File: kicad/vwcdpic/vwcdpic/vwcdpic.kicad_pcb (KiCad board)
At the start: 2 copper layers, 14.6 x 13.1 mm, 11 parts, among them U1 PIC12F629, U2 LM78L05ACZ

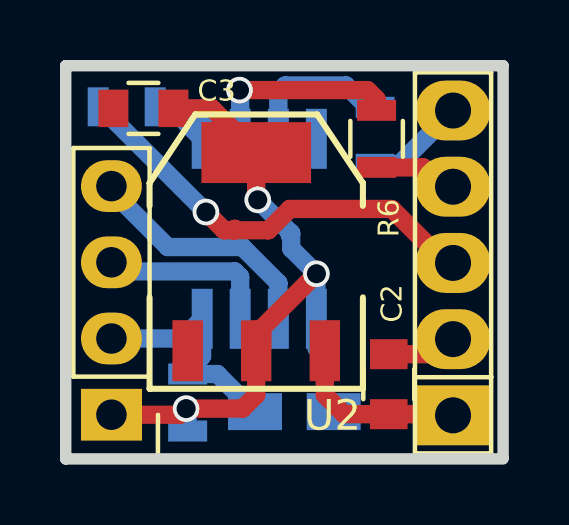
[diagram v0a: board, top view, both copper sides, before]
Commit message: 78L05 int SOT23 package as alternative to AM1117
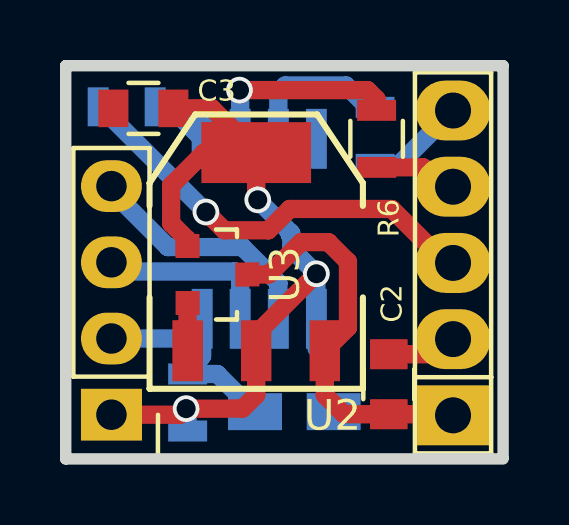
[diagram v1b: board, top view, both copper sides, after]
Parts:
- added U3: MC78L05ACH, Housings_SOT-23_SOT-143_TSOT-6:SOT-23, F.Cu at (142.8, 121.3)
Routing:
- net POWER_CTL: track 6.18 -> 13.5 mm
- net +5V: track 21.9 -> 27.5 mm
- net GND: track 2.40 -> 3.99 mm
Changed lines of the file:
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@@
-(kicad_pcb (version 4) (host pcbnew 0.201508250901+6122~28~ubuntu14.04.1-product)
+(kicad_pcb (version 4) (host pcbnew 0.201510080346+6253~30~ubuntu14.04.1-product)
   (general
-    (links 23)
+    (links 26)
     (no_connects 0)
     (area 137.579099 114.160299 152.539701 127.647701)
     (thickness 1.6002)
     (drawings 6)
-    (tracks 85)
+    (tracks 96)
     (zones 0)
-    (modules 11)
+    (modules 12)
     (nets 13)
   )
@@
     (34 B.Paste user hide)
     (35 F.Paste user hide)
-    (36 B.SilkS user hide)
+    (36 B.SilkS user)
     (37 F.SilkS user)
-    (38 B.Mask user hide)
-    (39 F.Mask user hide)
+    (38 B.Mask user)
+    (39 F.Mask user)
     (40 Dwgs.User user)
     (44 Edge.Cuts user)
@@
     (pad 5 thru_hole oval (at 5.08 0 90) (size 2 2.5) (drill 1.2) (layers *.Cu *.Mask F.SilkS)
       (net 11 CLK-PRG_DATA))
-    (model Pin_Headers/Pin_Header_Straight_1x05.wrl
+    (model Pin_Headers.3dshapes/Pin_Header_Straight_1x05.wrl
       (at (xyz 0 0 0))
       (scale (xyz 1 1 1))
@@
     (pad 4 smd rect (at 1.905 -3 180) (size 0.7 2) (layers Back B.Paste B.Mask)
       (net 8 RESET))
-    (model smd/cms_so8.wrl
-      (at (xyz 0 0 0))
-      (scale (xyz 0.5 0.32 0.5))
+    (model Housings_SOIC.3dshapes/SOIJ-8_5.3x5.3mm_Pitch1.27mm.wrl
+      (at (xyz 0 0 0))
+      (scale (xyz 1 1 1))
       (rotate (xyz 0 0 0))
     )
@@
     (pad GND smd rect (at -2.286 3.302) (size 1.016 2.032) (layers Front F.Paste F.Mask)
       (net 2 GND))
-    (model smd/SOT223.wrl
-      (at (xyz 0 0 0))
-      (scale (xyz 0.4 0.4 0.4))
+    (model /home/nail/src/kicad/KiCad/3d_models/ab2_sot/AB2_SOT223.wrl
+      (at (xyz 0 0 0))
+      (scale (xyz 1 1 1))
+      (rotate (xyz 0 0 0))
+    )
+  )
+  (module Housings_SOT-23_SOT-143_TSOT-6:SOT-23 (layer Front)
+    (at 142.82928 121.3104 270)
+    (descr "SOT-23, Standard")
+    (tags SOT-23)
+    (attr smd)
+    (fp_text reference U3 (at 0 -2.25 270) (layer F.SilkS)
+      (effects (font (size 1 1) (thickness 0.15)))
+    )
+    (fp_text value MC78L05ACH (at 0 2.3 270) (layer F.Fab)
+      (effects (font (size 1 1) (thickness 0.15)))
+    )
+    (fp_line (start -1.65 -1.6) (end 1.65 -1.6) (layer F.CrtYd) (width 0.05))
+    (fp_line (start 1.65 -1.6) (end 1.65 1.6) (layer F.CrtYd) (width 0.05))
+    (fp_line (start 1.65 1.6) (end -1.65 1.6) (layer F.CrtYd) (width 0.05))
+    (fp_line (start -1.65 1.6) (end -1.65 -1.6) (layer F.CrtYd) (width 0.05))
+    (fp_line (start 1.29916 -0.65024) (end 1.2509 -0.65024) (layer F.SilkS) (width 0.15))
+    (fp_line (start -1.49982 0.0508) (end -1.49982 -0.65024) (layer F.SilkS) (width 0.15))
+    (fp_line (start -1.49982 -0.65024) (end -1.2509 -0.65024) (layer F.SilkS) (width 0.15))
+    (fp_line (start 1.29916 -0.65024) (end 1.49982 -0.65024) (layer F.SilkS) (width 0.15))
+    (fp_line (start 1.49982 -0.65024) (end 1.49982 0.0508) (layer F.SilkS) (width 0.15))
+    (pad 1 smd rect (at -0.95 1.00076 270) (size 0.8001 0.8001) (layers Front F.Paste F.Mask)
+      (net 1 +5V))
+    (pad 2 smd rect (at 0.95 1.00076 270) (size 0.8001 0.8001) (layers Front F.Paste F.Mask)
+      (net 2 GND))
+    (pad 3 smd rect (at 0 -0.99822 270) (size 0.8001 0.8001) (layers Front F.Paste F.Mask)
+      (net 3 POWER_CTL))
+    (model Housings_SOT-23_SOT-143_TSOT-6.3dshapes/SOT-23.wrl
+      (at (xyz 0 0 0))
+      (scale (xyz 1 1 1))
       (rotate (xyz 0 0 0))
     )
@@
   (gr_line (start 137.7696 114.3508) (end 152.3492 114.3508) (angle 90) (layer Edge.Cuts) (width 0.381))
   (gr_line (start 152.3492 114.3508) (end 152.3492 127.4064) (angle 90) (layer Edge.Cuts) (width 0.381))
+  (segment (start 141.82852 120.3604) (end 141.82852 120.14708) (width 0.6096) (layer Front) (net 1) (status C00000))
+  (segment (start 141.82852 120.14708) (end 141.28496 119.60352) (width 0.6096) (layer Front) (net 1) (status 400000))
+  (segment (start 141.28496 119.60352) (end 141.28496 118.34368) (width 0.6096) (layer Front) (net 1))
+  (segment (start 141.28496 118.34368) (end 142.38224 117.2464) (width 0.6096) (layer Front) (net 1) (status 800000))
+  (segment (start 142.38224 117.2464) (end 144.1196 117.2464) (width 0.6096) (layer Front) (net 1) (status C00000))
   (segment (start 141.3604 115.7732) (end 142.6464 115.7732) (width 0.6096) (layer Front) (net 1))
   (segment (start 142.6464 115.7732) (end 144.1196 117.2464) (width 0.6096) (layer Front) (net 1))
@@
   (via (at 141.7828 125.7808) (size 0.889) (drill 0.635) (layers Front Back) (net 1))
   (segment (start 141.5796 125.984) (end 141.7828 125.7808) (width 0.6096) (layer Front) (net 1))
+  (segment (start 141.82852 122.2604) (end 141.82852 123.84532) (width 0.6096) (layer Front) (net 2) (status C00000))
+  (segment (start 141.82852 123.84532) (end 141.8336 123.8504) (width 0.6096) (layer Front) (net 2) (status C00000))
   (segment (start 148.5392 123.968) (end 150.17674 123.968) (width 0.6096) (layer Front) (net 2))
   (segment (start 150.17674 123.968) (end 150.68042 123.46432) (width 0.6096) (layer Front) (net 2))
   (segment (start 141.8336 123.7996) (end 141.8336 123.8504) (width 0.6096) (layer Front) (net 2))
+  (segment (start 143.8275 121.3104) (end 144.53616 121.3104) (width 0.6096) (layer Front) (net 3) (status 400000))
+  (segment (start 147.17776 123.07824) (end 146.4056 123.8504) (width 0.6096) (layer Front) (net 3) (status 800000))
+  (segment (start 147.17776 120.88368) (end 147.17776 123.07824) (width 0.6096) (layer Front) (net 3))
+  (segment (start 146.52752 120.23344) (end 147.17776 120.88368) (width 0.6096) (layer Front) (net 3))
+  (segment (start 145.61312 120.23344) (end 146.52752 120.23344) (width 0.6096) (layer Front) (net 3))
+  (segment (start 144.53616 121.3104) (end 145.61312 120.23344) (width 0.6096) (layer Front) (net 3))
   (segment (start 148.5392 125.968) (end 150.6441 125.968) (width 0.6096) (layer Front) (net 3))
   (segment (start 150.6441 125.968) (end 150.68042 126.00432) (width 0.6096) (layer Front) (net 3))
@@
   (segment (start 141.2522 115.7224) (end 142.3162 116.7864) (width 0.6096) (layer Back) (net 4))
   (segment (start 140.7516 115.7224) (end 141.2522 115.7224) (width 0.6096) (layer Back) (net 4))
-  (segment (start 138.8516 115.7224) (end 138.938 115.7224) (width 0.6096) (layer Back) (net 5))
+  (segment (start 142.4432 119.2276) (end 142.44828 119.2276) (width 0.6096) (layer Front) (net 5))
+  (segment (start 143.05788 119.8372) (end 144.526 119.8372) (width 0.6096) (layer Front) (net 5))
+  (segment (start 142.44828 119.2276) (end 143.05788 119.8372) (width 0.6096) (layer Front) (net 5))
   (segment (start 138.938 115.7224) (end 142.4432 119.2276) (width 0.6096) (layer Back) (net 5))
-  (segment (start 143.4084 119.7864) (end 143.4084 119.8372) (width 0.6096) (layer Front) (net 5))
-  (segment (start 143.3576 119.8372) (end 143.4084 119.7864) (width 0.6096) (layer Front) (net 5))
-  (segment (start 143.0528 119.8372) (end 143.3576 119.8372) (width 0.6096) (layer Front) (net 5))
-  (segment (start 142.4432 119.2276) (end 143.0528 119.8372) (width 0.6096) (layer Front) (net 5))
   (via (at 142.4432 119.2276) (size 0.889) (drill 0.635) (layers Front Back) (net 5))
-  (segment (start 150.68042 120.92432) (end 150.43912 120.92432) (width 0.6096) (layer Front) (net 5))
   (segment (start 150.43912 120.92432) (end 148.6408 119.126) (width 0.6096) (layer Front) (net 5))
-  (segment (start 144.526 119.8372) (end 143.4084 119.8372) (width 0.6096) (layer Front) (net 5))
   (segment (start 145.2372 119.126) (end 144.526 119.8372) (width 0.6096) (layer Front) (net 5))
   (segment (start 148.6408 119.126) (end 145.2372 119.126) (width 0.6096) (layer Front) (net 5))
+  (segment (start 138.8516 115.7224) (end 138.938 115.7224) (width 0.6096) (layer Back) (net 5))
+  (segment (start 150.68042 120.92432) (end 150.43912 120.92432) (width 0.6096) (layer Front) (net 5))
   (segment (start 150.68042 120.92432) (end 150.54072 120.92432) (width 0.6096) (layer Front) (net 5))
   (segment (start 150.68042 120.92432) (end 150.48992 120.92432) (width 0.6096) (layer Front) (net 5))
